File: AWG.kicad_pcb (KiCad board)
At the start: 2 copper layers, 140 x 75 mm, 80 parts, among them J1001 Conn_01x03, J1002 Conn_01x05, J1003 Conn_01x06, J1005 Conn_01x01, J1006 Conn_01x01, J1007 Conn_01x01, J1008 Conn_01x01, J1009 Conn_01x01, J1010 Conn_01x01, J1011 Conn_01x01, J1012 Conn_01x01, J1013 Conn_01x05, J2 Conn afficheur, J5 SMA, Q1001 NTE2633, Q1002 NTE2634, U1 Pico, U1001 L7812, U1002 L7912, U1003 L7805, U1004 L7905, U3 AD8055ARZ

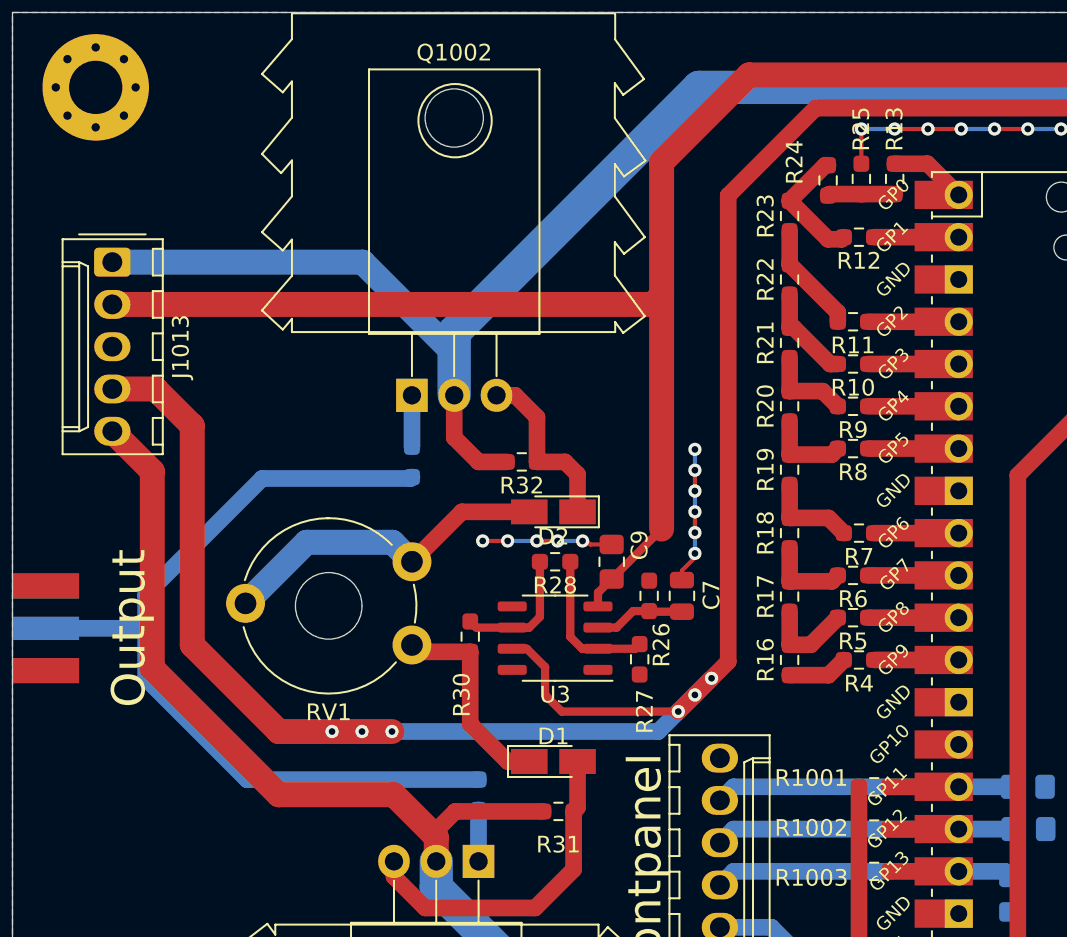
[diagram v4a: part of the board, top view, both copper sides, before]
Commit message: 1mf non polar cap added
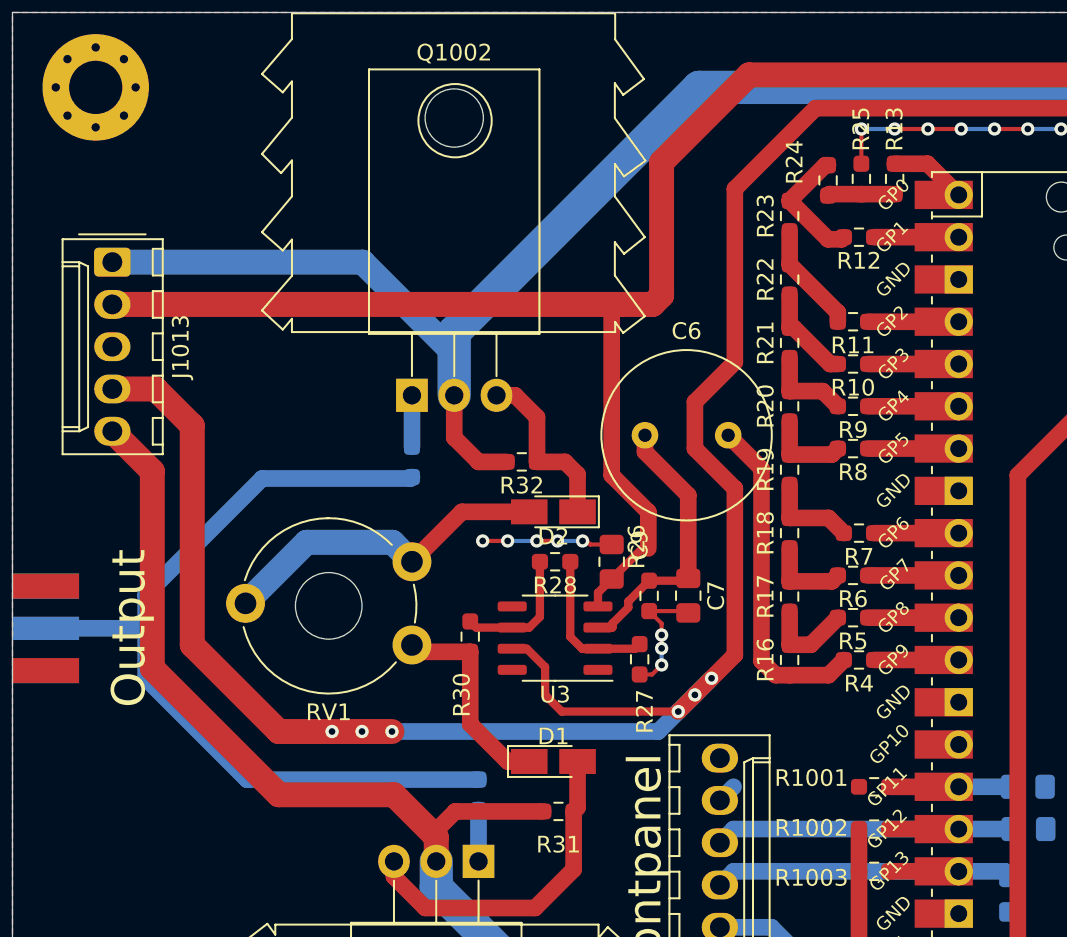
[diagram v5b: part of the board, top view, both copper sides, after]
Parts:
- added C6: 1mF, Capacitor_THT:C_Radial_D10.0mm_H16.0mm_P5.00mm, F.Cu at (178.0, 75.4)
- C7: footprint Capacitor_SMD:C_0805_2012Metric -> Capacitor_SMD:C_0805_2012Metric_Pad1.18x1.45mm_HandSolder
- moved C7 0.38 mm to (180.6, 85.0), turned to 270 degrees
- turned R26 to 270 degrees
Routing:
- net Net-(C6-Pad2): track 3.63 -> 20.1 mm
- net Net-(C1017-Pad1): track 22.0 -> 8.44 mm
- net Net-(C6-Pad1): track 5.47 -> 16.7 mm
- net +3V3: track 89.2 -> 86.7 mm
- net +5V: track 242.2 -> 244.2 mm
- net GND: track 57.1 -> 56.4 mm, vias 30 -> 27

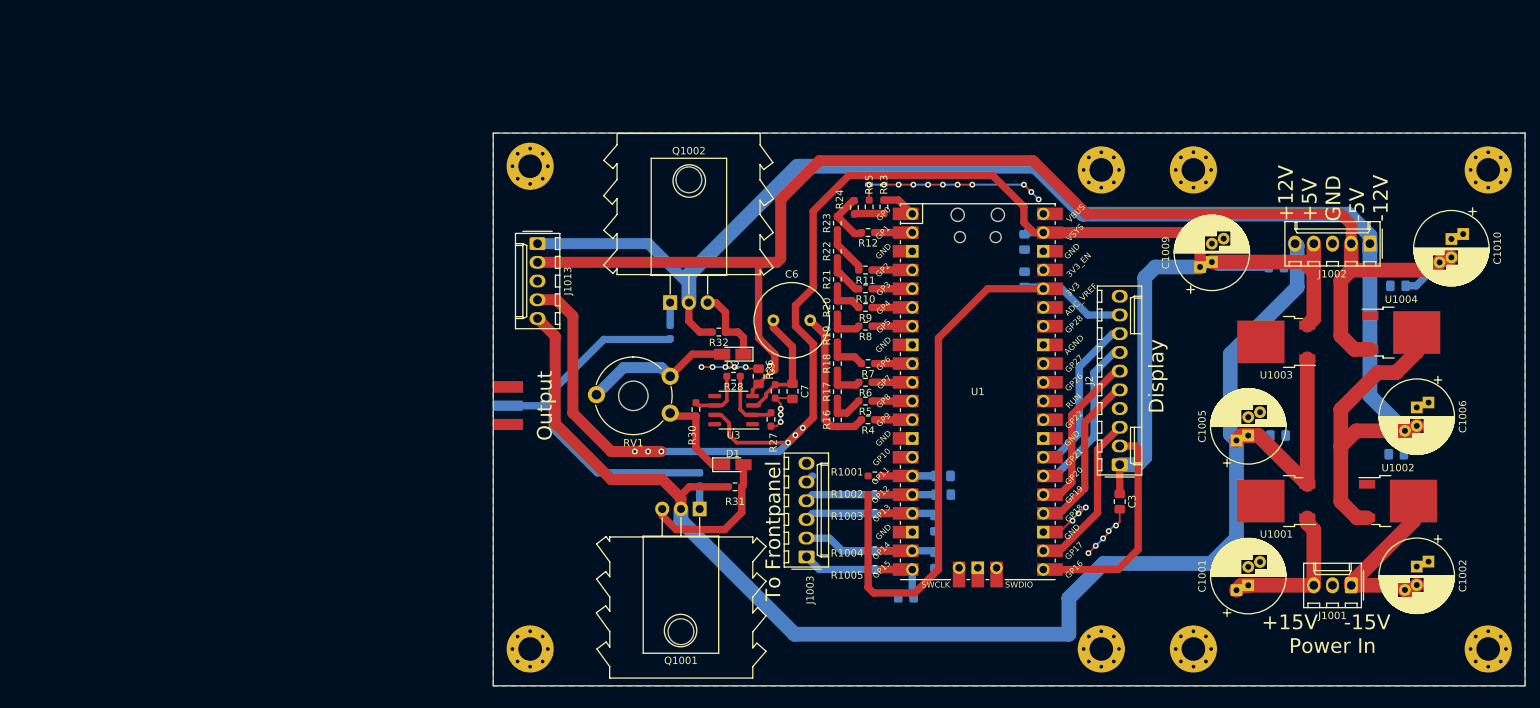
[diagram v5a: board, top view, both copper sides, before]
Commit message: minor cosmetic details.Bypass cap changed
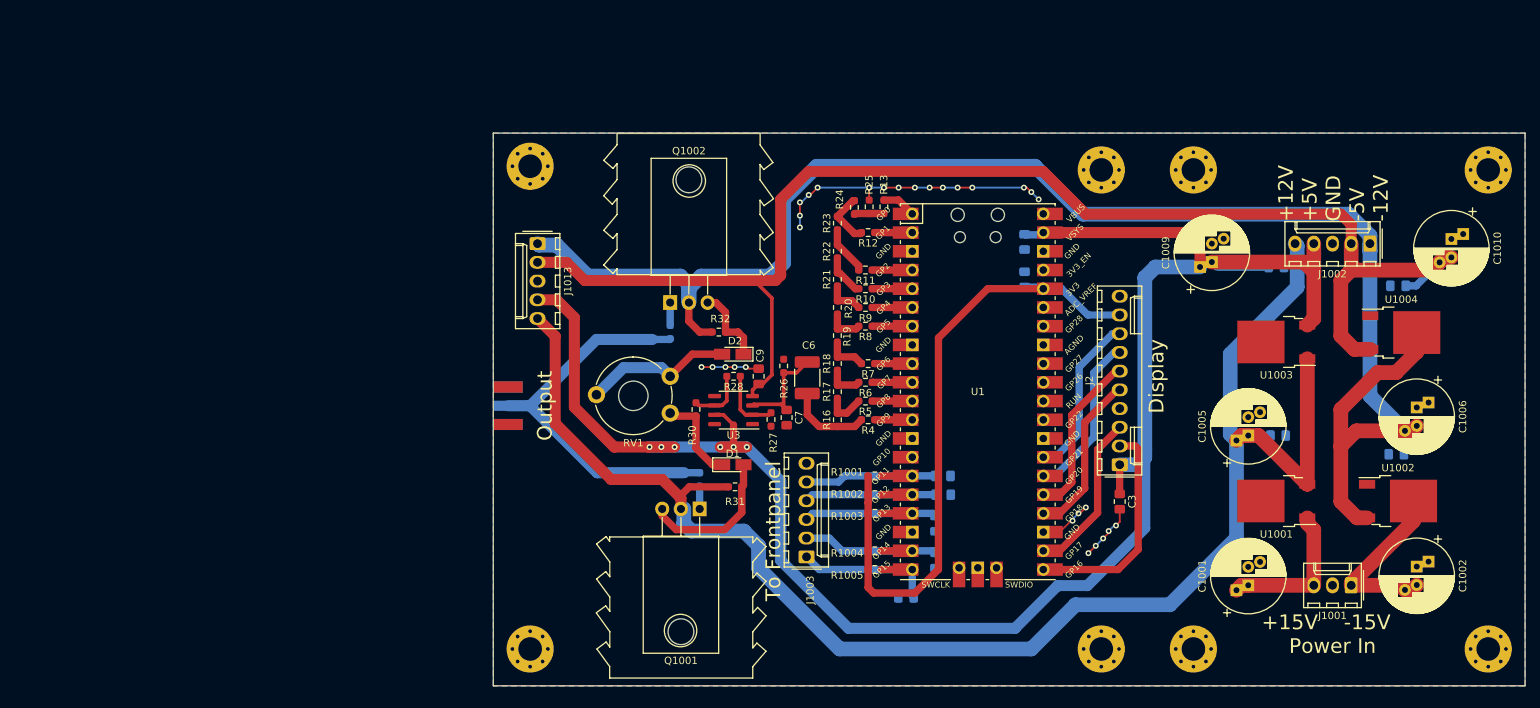
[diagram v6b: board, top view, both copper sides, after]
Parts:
- C6: footprint Capacitor_THT:C_Radial_D10.0mm_H16.0mm_P5.00mm -> Capacitor_SMD:C_1812_4532Metric_Pad1.57x3.40mm_HandSolder
- moved C6 9.06 mm to (182.6, 83.2), turned to 270 degrees
- moved C7 3.65 mm to (179.8, 88.6)
- moved R26 3.64 mm to (179.4, 81.6), turned to 90 degrees
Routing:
- net Net-(C1017-Pad1): track 8.44 -> 22.0 mm
- net Net-(C6-Pad2): track 20.1 -> 11.3 mm
- net Net-(J5-Pad1): track 52.5 -> 61.1 mm
- net GND: track 56.4 -> 62.0 mm, vias 27 -> 29
- net -12V: track 216.7 -> 220.7 mm
- net Net-(C6-Pad1): track 16.7 -> 14.0 mm
- net +3V3: track 86.7 -> 89.2 mm
- net -5V: track 185.8 -> 187.7 mm
- net +5V: track 244.2 -> 246.0 mm
- net +12V: track 213.6 -> 214.4 mm

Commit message: schematic and 3Dview added in documents folder
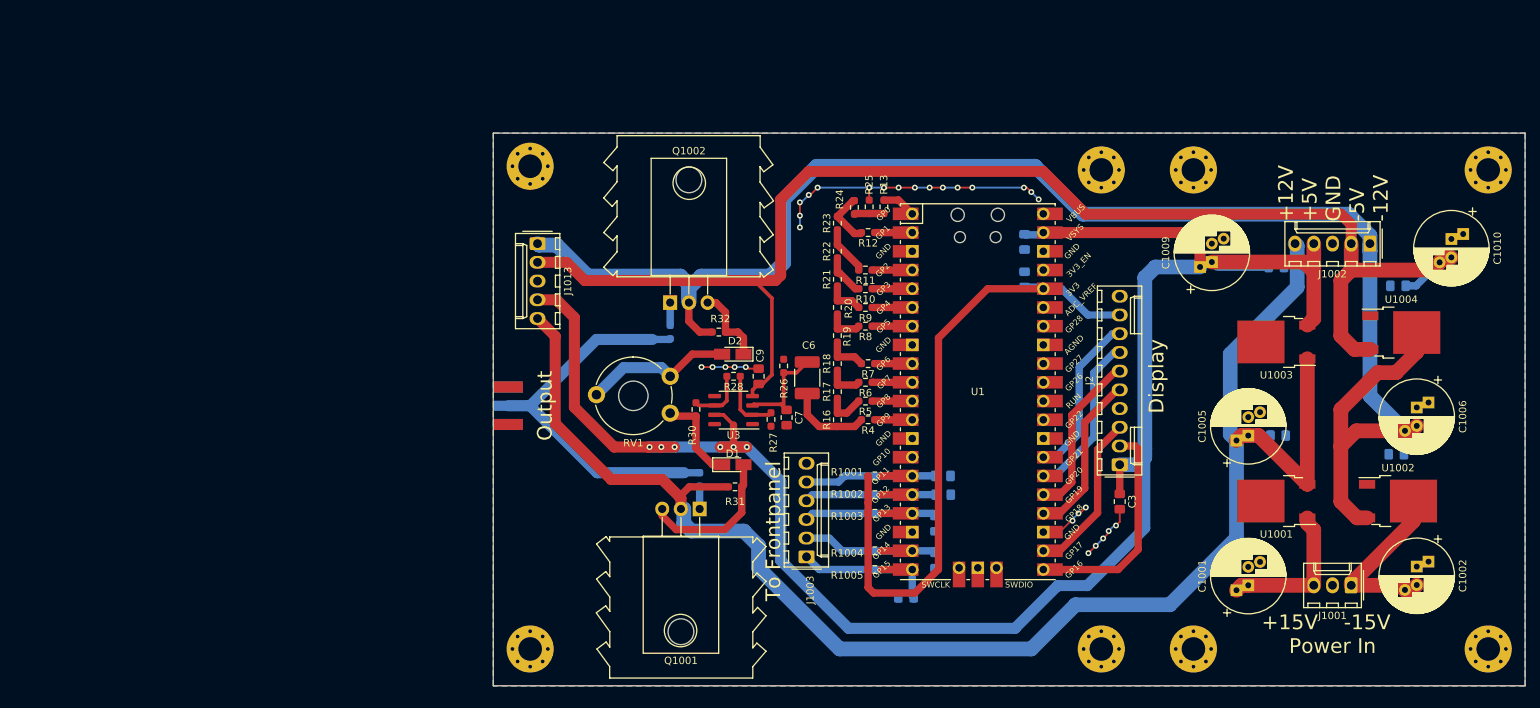
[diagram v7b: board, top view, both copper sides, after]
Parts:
- moved HS1002 0.30 mm to (166.5, 56.8)

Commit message: iBOM added
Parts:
- added REF**: OSHW-Logo2_7.3x6mm_SilkScreen, Symbol:OSHW-Logo2_7.3x6mm_SilkScreen, B.Cu at (202.0, 80.0)
- added REF**: KiCad-Logo2_5mm_SilkScreen, Symbol:KiCad-Logo2_5mm_SilkScreen, B.Cu at (210.0, 80.0)
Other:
- board text added: "Arbitrary Waveform Generator"
